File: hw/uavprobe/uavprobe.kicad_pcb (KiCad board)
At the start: 2 copper layers, 31 x 120 mm, 123 parts, among them IC1 UCLAMP3306P.TCT, J1 USB_C_Receptacle_USB2.0_14P, J10 SERIAL1 (flow), J11 SERIAL1 (GPS/I2C), J12 SERIAL1 (Lidar), J13 I^{2}C (Lidar), J14 I^{2}C, J15 USB2, J16 CAN1, J17 CAN2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

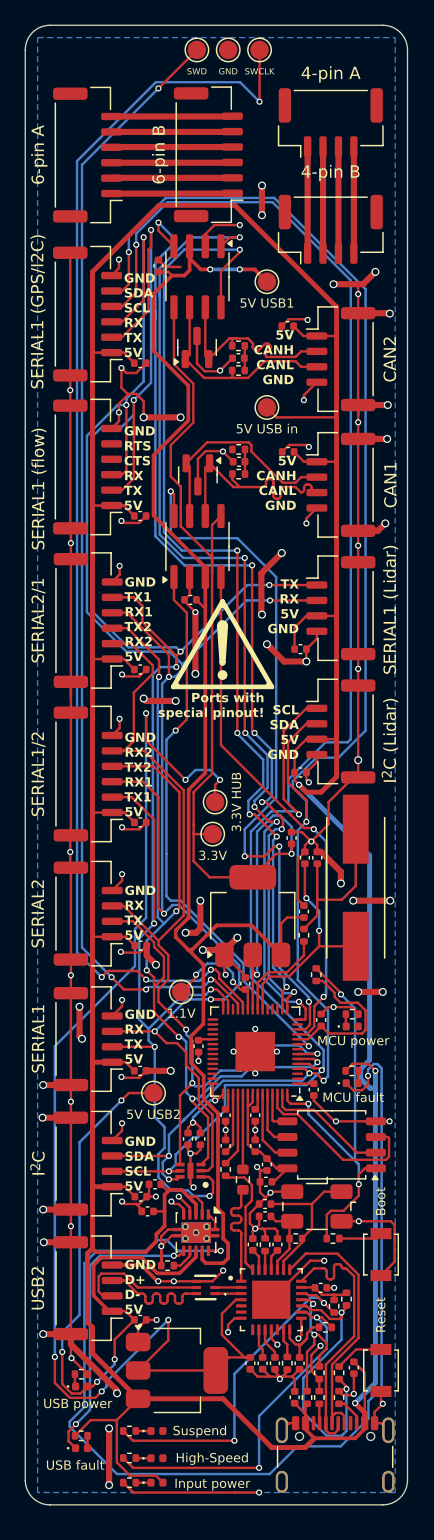
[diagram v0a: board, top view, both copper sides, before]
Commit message: Layout 2
Honoring the DRC and with a new uSB-C connector
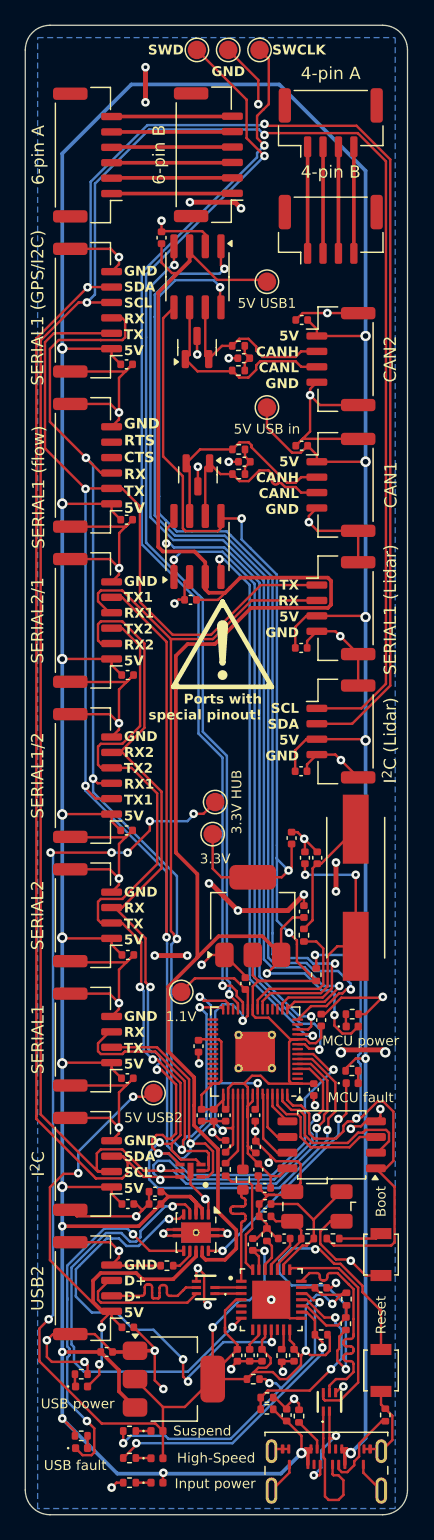
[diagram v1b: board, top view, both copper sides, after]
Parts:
- added FL2: ECLAMP8052P.TCT, Import:ECLAMP8052PTCT, F.Cu at (132.3, 137.1)
- J1: footprint Connector_USB:USB_C_Receptacle_GCT_USB4105-xx-A_16P_TopMnt_Horizontal -> Connector_USB:USB_C_Receptacle_Amphenol_124019772112A
- R6, R7, R8, R9: value 60 -> 60R
- U3: footprint Package_DFN_QFN:QFN-56-1EP_7x7mm_P0.4mm_EP3.2x3.2mm -> Package_DFN_QFN:QFN-56-1EP_7x7mm_P0.4mm_EP3.2x3.2mm_ThermalVias
- Y1: value ABLS-12.000MHZ-B4-T -> 12 MHz
- moved C23 15.7 mm to (114.2, 133.1), turned to 0 degrees
- moved R25 8.83 mm to (126.1, 135.2), turned to 0 degrees
- moved C22 6.67 mm to (128.8, 138.2), turned to 90 degrees
- moved R14 4.70 mm to (127.2, 136.8), turned to 180 degrees
- moved R15 4.02 mm to (133.6, 130.8), turned to 90 degrees
- moved R12 4.01 mm to (136.8, 138.2)
- moved R13 3.39 mm to (127.2, 137.7), turned to 180 degrees
- moved C18 2.30 mm to (118.7, 42.7)
- moved R11 2.24 mm to (129.8, 138.2)
- moved C13 2.21 mm to (122.9, 113.8)
- moved C14 2.21 mm to (121.9, 113.8)
- moved J1 1.76 mm to (132.0, 144.1)
- moved C30 1.29 mm to (115.9, 100.8)
- moved C32 1.29 mm to (115.8, 90.8)
- moved C40 1.24 mm to (130.0, 49.4)
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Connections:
- U8 pad 21: /USB/USBC_D- -> /USB/USBIN_D-
- U8 pad 22: /USB/USBC_D+ -> /USB/USBIN_D+
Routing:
- net GND: track 419.1 -> 319.1 mm, vias 105 -> 61
- net /USB/FAULT1: track 88.4 -> 19.0 mm
- net /Connectors/I2C_SDA: track 134.6 -> 199.8 mm, vias 6 -> 4
- net /Connectors/I2C_SCL: track 137.5 -> 196.2 mm
- net /RP2040/VBUS1: track 118.8 -> 157.1 mm
- net /USB/USBPWREN1: track 3.70 -> 36.6 mm
- net /USB/USBPWREN2: track 3.10 -> 35.5 mm, vias 2 -> 4
- net /Connectors/VBUS: track 337.7 -> 368.8 mm, vias 3 -> 18
- net Net-(R15-Pad1): track 3.97 -> 30.9 mm, vias 0 -> 2
- net +3.3V (HUB): track 118.1 -> 140.2 mm, vias 6 -> 10
- net +1.1V: track 15.3 -> 33.7 mm, vias 2 -> 3
- net /USB/USBIN_D+: track 0.00 -> 17.9 mm
- net /USB/USBIN_D-: track 0.00 -> 17.8 mm
- net /USB/~{RESET}: track 23.2 -> 5.54 mm, vias 2 -> 0
- net Net-(U3-SWCLK): track 103.7 -> 86.7 mm, vias 4 -> 2
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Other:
- board size 31 x 120 mm -> 31 x 120.8 mm

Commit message: Edge cleaning
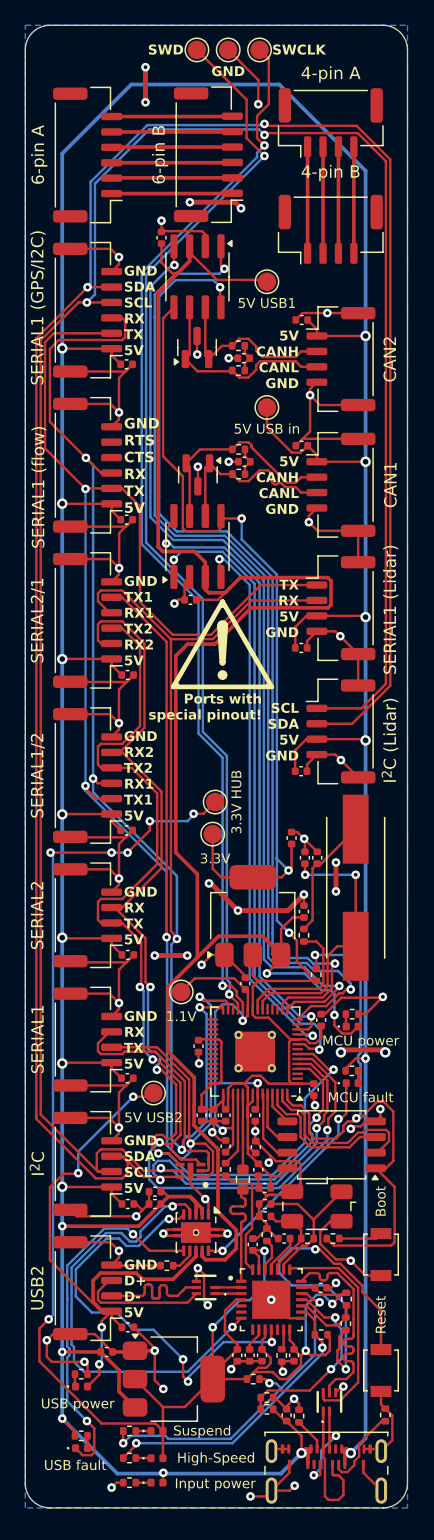
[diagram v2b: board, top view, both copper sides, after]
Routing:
- net GND: track 319.1 -> 323.1 mm, vias 61 -> 63
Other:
- board size 31 x 120.8 mm -> 31 x 120.2 mm
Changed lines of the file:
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@@
 	)
 	(gr_line
-		(start 136.6 146.25)
-		(end 109.6 146.25)
+		(start 136.6 145.7)
+		(end 109.6 145.7)
 		(stroke
 			(width 0.1)
@@
 	(gr_line
 		(start 138.6 27.45)
-		(end 138.6 144.25)
+		(end 138.6 143.7)
 		(stroke
 			(width 0.1)
@@
 	)
 	(gr_arc
-		(start 138.6 144.25)
-		(mid 138.014214 145.664214)
-		(end 136.6 146.25)
+		(start 138.6 143.7)
+		(mid 138.014214 145.114214)
+		(end 136.6 145.7)
 		(stroke
 			(width 0.1)
@@
 	)
 	(gr_arc
-		(start 109.6 146.25)
-		(mid 108.185786 145.664214)
-		(end 107.6 144.25)
+		(start 109.6 145.7)
+		(mid 108.185786 145.114214)
+		(end 107.6 143.7)
 		(stroke
 			(width 0.1)
@@
 	)
 	(gr_line
-		(start 107.6 144.25)
+		(start 107.6 143.7)
 		(end 107.6 27.45)
 		(stroke
@@
 	)
 	(segment
+		(start 125.863245 144.766603)
+		(end 127.098397 144.766603)
+		(width 0.2)
+		(layer "F.Cu")
+		(net 1)
+	)
+	(segment
 		(start 132.794389 125.548001)
 		(end 133.898001 125.548001)
@@
 	)
 	(segment
+		(start 129.055 144.295)
+		(end 127.57 144.295)
+		(width 0.2)
+		(layer "F.Cu")
+		(net 1)
+	)
+	(segment
 		(start 115.819 78.711)
 		(end 116.09 78.44)
@@
 	)
 	(segment
+		(start 129.45 143.9)
+		(end 129.055 144.295)
+		(width 0.2)
+		(layer "F.Cu")
+		(net 1)
+	)
+	(segment
 		(start 132.05 127.85)
 		(end 132.4 127.85)
@@
 	)
 	(segment
+		(start 127.098397 144.766603)
+		(end 127.57 144.295)
+		(width 0.2)
+		(layer "F.Cu")
+		(net 1)
+	)
+	(segment
 		(start 121.9 114.33)
 		(end 123.85 114.33)
@@
 	)
 	(via
+		(at 129.45 143.9)
+		(size 0.7)
+		(drill 0.3)
+		(layers "F.Cu" "B.Cu")
+		(free yes)
+		(net 1)
+	)
+	(via
 		(at 133.4 135.85)
 		(size 0.7)
@@
 	)
 	(via
+		(at 125.863245 144.766603)
+		(size 0.7)
+		(drill 0.3)
+		(layers "F.Cu" "B.Cu")
+		(free yes)
+		(net 1)
+	)
+	(via
 		(at 127.35 117.7)
 		(size 0.7)
@@
 		(polygon
 			(pts
-				(xy 108.6 26.45) (xy 137.6 26.45) (xy 137.6 145.75) (xy 108.6 145.75)
+				(xy 107.6 25.45) (xy 138.6 25.45) (xy 138.6 145.7) (xy 107.6 145.7)
 			)
 		)
